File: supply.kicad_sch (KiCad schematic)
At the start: 92 parts, among them J6 205338-0004, J8 282834-4, Q5 PJE138K, Q6 SSM3J332R, Q8 PJE138K, SW1 SW_SPDT, U1 TPS56C230, U12 74LVC1G08, U13 74HCS74, U16 NTS0102, U17 SN74LV1T32DCKR, U29 TPS56C230, U41 NCP730BMT330, U42 TPS7A0518P, U6 ADM1176-1ARMZ-R7

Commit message: route all diff pairs, length tuning
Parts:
- removed R81: 10k, Resistor_SMD:R_0603_1608Metric, symbol Device:R_Small
- removed U16: NTS0102, Argus-IC:NXP_XSON-8, symbol JetsonCarrier:NTS0102
- added U30: NTS0102, Argus-IC:NXP_XSON-8, symbol Argus-IC:NTS0102
- renumbered BTN3 to BTN2, C8 to C70, C9 to C71, C26 to C72, C109 to C73, C56 to C74, C103 to C75, C57 to C76, C5 to C77, C58 to C78, C59 to C79, C65 to C80, C6 to C81, C76 to C82, C93 to C83, C77 to C84, C7 to C85, C105 to C86, C83 to C87, C102 to C88, C104 to C89, C106 to C90, C78 to C91, C80 to C92, C81 to C93, C82 to C94, C84 to C95, C85 to C96, C107 to C97, C90 to C98, C91 to C99, D7 to D19, D14 to D20, D16 to D21, D27 to D22, D25 to D23, D28 to D24, D26 to D25, J8 to J15, J6 to J16, Q8 to Q4, R14 to R104, R115 to R105, R1 to R106, R148 to R107, R25 to R108, R155 to R109, R62 to R110, R91 to R111, R193 to R112, R194 to R113, R153 to R114, R191 to R115, R82 to R116, R181 to R117, R156 to R118, R157 to R119, R158 to R120, R159 to R121, R160 to R122, R161 to R123, R162 to R124, R167 to R125, R163 to R126, R164 to R127, R165 to R128, R166 to R129, R170 to R130, R171 to R131, R168 to R132, R169 to R133, R172 to R134, R173 to R135, TP23 to TP21, TP21 to TP22, TP24 to TP23, TP28 to TP24, U12 to U27, U17 to U28, U6 to U29, U13 to U31, U1 to U32, U29 to U33, U41 to U34, U42 to U35
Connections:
- net 3V3_STDB: now also U30.3 (VCC_{A}), U30.6 (OE)
- net 5V_SoM: now also U30.7 (VCC_{B})
- net GND: now also U30.2 (GND)
- net POWER_EN: now also U30.8 (B_{1})
- net POWER_EN_3V3: now also U30.5 (A_{1})
- net SLEEP/~{WAKE}: now also U30.1 (B_{2})
- net SLEEP/~{WAKE}_3V3: now also U30.4 (A_{2})

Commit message: DRC cleanup
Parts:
- U31: footprint Package_DFN_QFN:DHWQFN-14-1EP_2.5x3mm_P0.5mm_EP1x1.5mm_ThermalVias -> Package_DFN_QFN:DHWQFN-14-1EP_2.5x3mm_P0.5mm_EP1x1.5mm
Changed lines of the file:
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@@
 			)
 		)
-		(property "Footprint" "Package_DFN_QFN:DHWQFN-14-1EP_2.5x3mm_P0.5mm_EP1x1.5mm_ThermalVias"
+		(property "Footprint" "Package_DFN_QFN:DHWQFN-14-1EP_2.5x3mm_P0.5mm_EP1x1.5mm"
 			(at 245.11 67.31 0)
 			(hide yes)
@@
 			)
 		)
-		(property "Footprint" "Package_DFN_QFN:DHWQFN-14-1EP_2.5x3mm_P0.5mm_EP1x1.5mm_ThermalVias"
+		(property "Footprint" "Package_DFN_QFN:DHWQFN-14-1EP_2.5x3mm_P0.5mm_EP1x1.5mm"
 			(at 245.11 29.21 0)
 			(hide yes)
@@
 			)
 		)
-		(property "Footprint" "Package_DFN_QFN:DHWQFN-14-1EP_2.5x3mm_P0.5mm_EP1x1.5mm_ThermalVias"
+		(property "Footprint" "Package_DFN_QFN:DHWQFN-14-1EP_2.5x3mm_P0.5mm_EP1x1.5mm"
 			(at 183.515 54.61 0)
 			(hide yes)

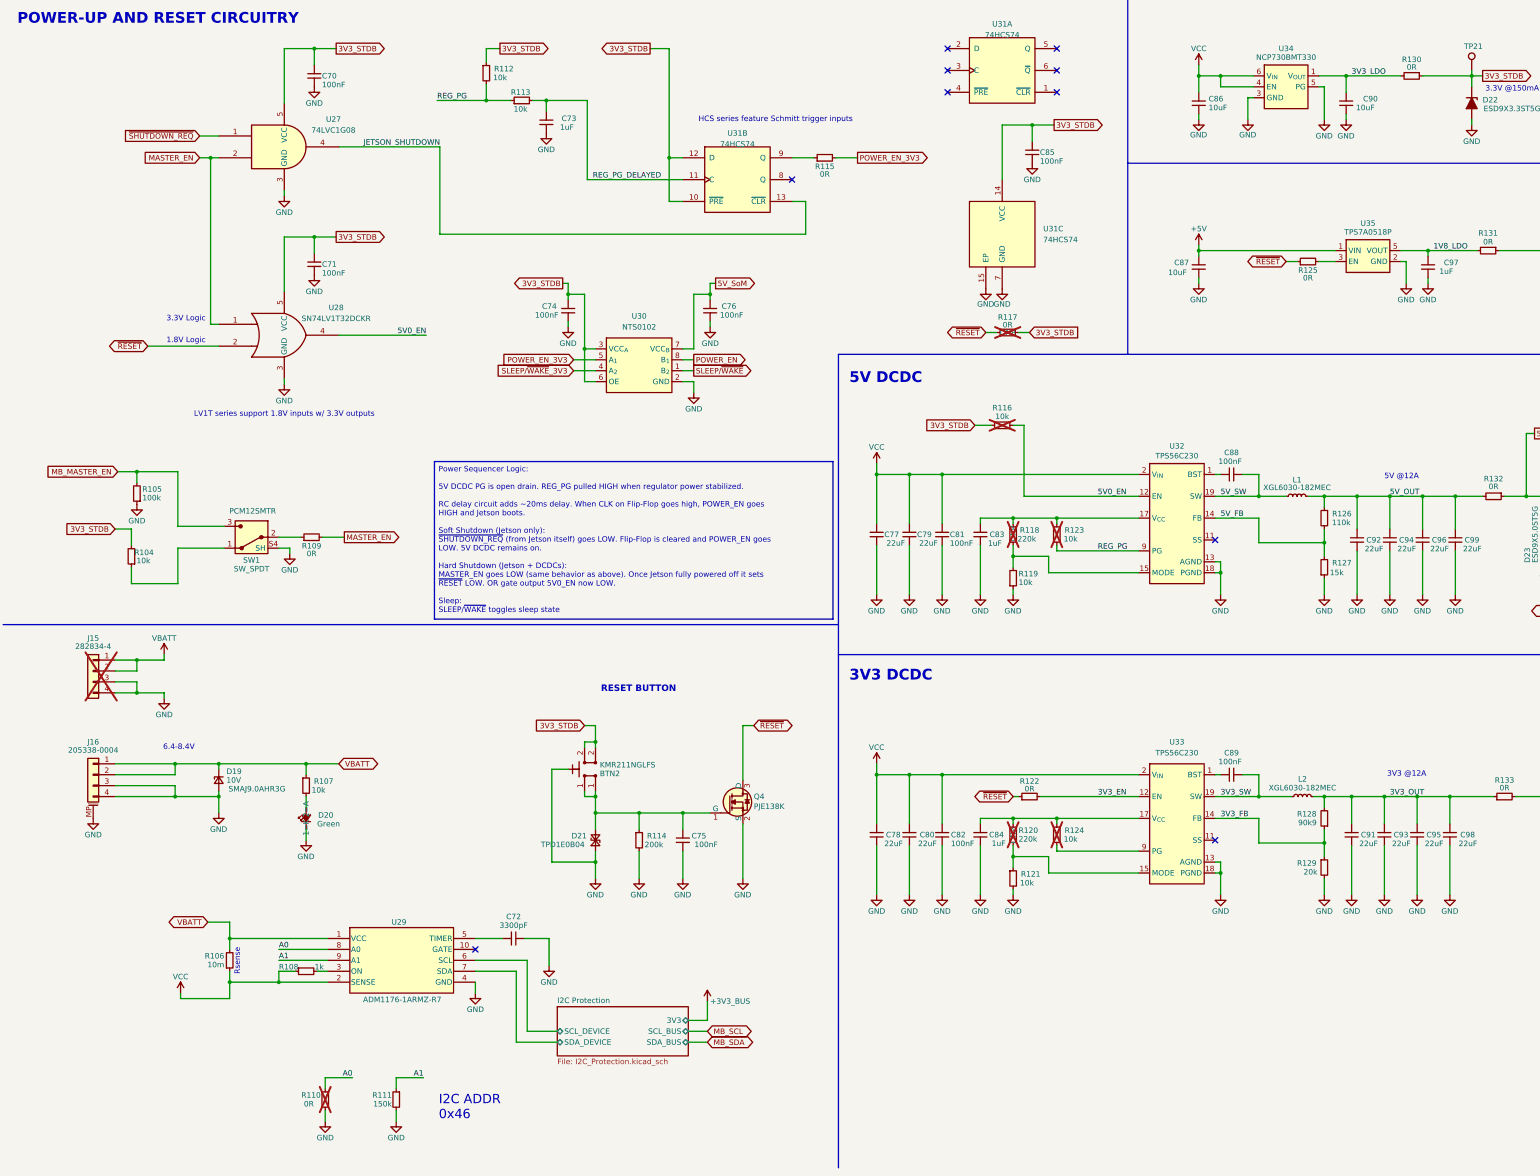
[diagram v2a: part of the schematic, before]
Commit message: Replace current monitor w/ INA226 (addr = 0x42)
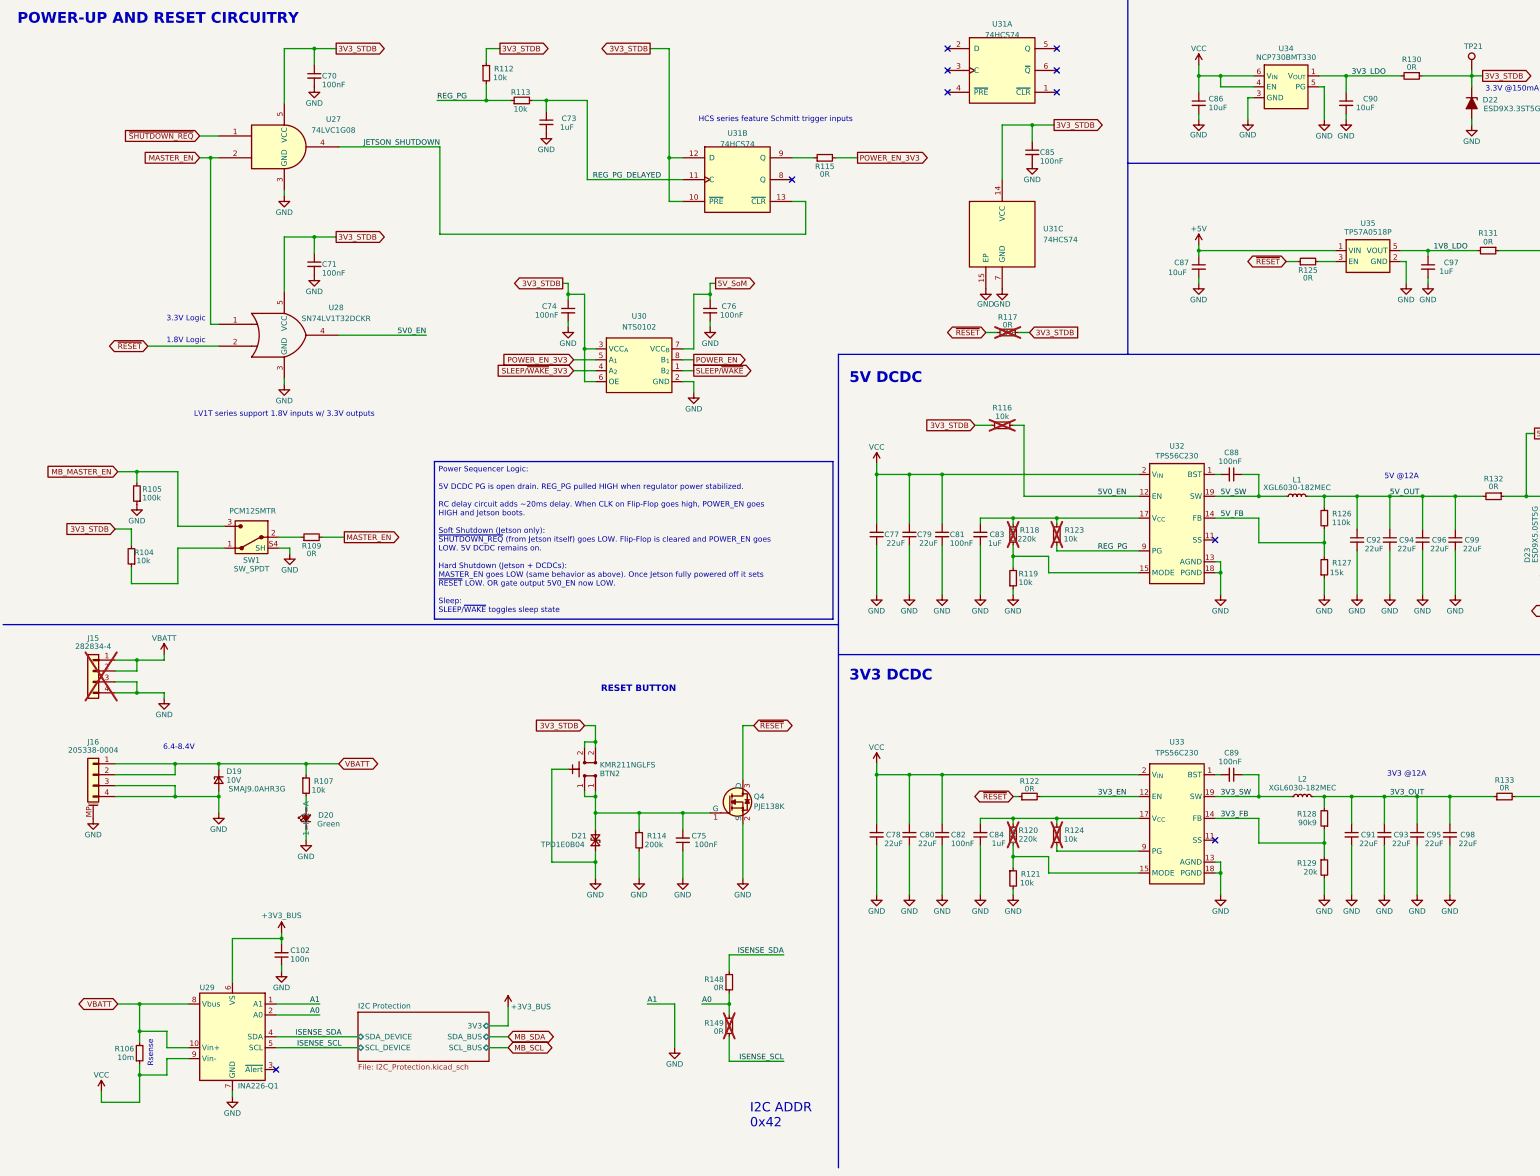
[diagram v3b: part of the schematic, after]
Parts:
- removed C72: 3300pF, Capacitor_SMD:C_0603_1608Metric, symbol Device:C_Small
- removed R108: 1k, Resistor_SMD:R_0603_1608Metric, symbol Device:R_Small
- removed R110: 0R, Resistor_SMD:R_0603_1608Metric, symbol Device:R_Small
- removed R111: 150k, Resistor_SMD:R_0603_1608Metric, symbol Device:R_Small
- removed U29: ADM1176-1ARMZ-R7, Package_SO:MSOP-10_3x3mm_P0.5mm, symbol JetsonCarrier:ADM1176-1ARMZ-R7
- added C102: 100n, Capacitor_SMD:C_0603_1608Metric, symbol Device:C_Small
- added R148, R149: 0R, Resistor_SMD:R_0603_1608Metric, symbol Device:R_Small
- added U29: INA226-Q1, Package_SO:TSSOP-10_3x3mm_P0.5mm, symbol Sensor_Energy:INA226
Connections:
- net +3V3_BUS: now also C102.2, U29.6 (VS)
- net A0: now also R148.1, R149.2, U29.2 (A0)
- net GND: now also C102.1, U29.1 (A1), U29.7 (GND)
- net VBATT: now also U29.10 (Vin+), U29.8 (Vbus)
- net VCC: now also U29.9 (Vin-)
- new net ISENSE_SCL: R149.1, U29.5 (SCL)
- new net ISENSE_SDA: R148.2, U29.4 (SDA)
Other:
- note added: "I2C ADDR 0x42"
- note removed: "I2C ADDR 0x46"
- moved on the sheet: R106

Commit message: Clean up silk, BOM
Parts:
- D20: Color Green -> Red
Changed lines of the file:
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@@
 			)
 		)
-		(property "Color" "Green"
+		(property "Color" "Red"
 			(at 91.059 204.47 90)
 			(show_name no)

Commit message: Final cleanup, production files
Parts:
- removed Q4, Q5: PJE138K, Package_TO_SOT_SMD:SOT-523, symbol JetsonCarrier:PJE138K
- added Q4, Q5: 2N7002, Package_TO_SOT_SMD:SOT-23, symbol Transistor_FET:2N7002
- C102: value 100n -> 100nF
- D24: value ESD1V8WT -> ESD5Z2.5T1G
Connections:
- net GND: now also Q4.2 (S), Q5.2 (S)
- net ~{RESET}: now also Q4.3 (D), Q5.1 (G)
- net at Q6.1 (G), R134.2: now also Q5.3 (D)
- net at BTN2.1, C75.2, D21.2 (A2)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: now also Q4.1 (G)

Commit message: Final BOM changes, gerbers
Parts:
- BTN2: LCSC (none) -> C221676
- C102, C70, C71, C74, C75, C76, C81, C82, C85, C88, C89: LCSC (none) -> C14663
- C73, C83, C84, C97: LCSC (none) -> C15849
- C77, C78, C79, C80: LCSC (none) -> C45783
- C86, C87, C90: LCSC (none) -> C96446
- C91, C92, C93, C94, C95, C96, C98, C99: LCSC (none) -> C84419
- D19: LCSC (none) -> C3720382
- D20: LCSC (none) -> C2286
- D21: LCSC (none) -> C1975594
- D22, D25: LCSC (none) -> C130456
- D23: LCSC (none) -> C87910
- D24: LCSC (none) -> C890620
- J16: LCSC (none) -> C916325
- L1, L2: value XGL6030-182MEC -> Pulse_PM2205; footprint Inductor_SMD:L_Coilcraft_XAL6030-XXX -> Argus-Passives:Pulse_PM2205; LCSC (none) -> C2638799
- Q4, Q5: LCSC (none) -> C8545
- Q6: LCSC (none) -> C146367
- R104, R107, R112, R113, R116, R119, R121, R123, R124, R134: LCSC (none) -> C25804
- R105: LCSC (none) -> C25803
- R106: LCSC (none) -> C108943
- R109, R115, R122, R125, R130, R131, R148, R149: LCSC (none) -> C21189
- R114: LCSC (none) -> C25811
- R117: LCSC (none) -> C17168
- R118, R120: LCSC (none) -> C22961
- R126: LCSC (none) -> C25574
- R127: LCSC (none) -> C22809
- R128: LCSC (none) -> C23129
- R129: LCSC (none) -> C4184
- R132, R133, R135: LCSC (none) -> C17477
- SW1: LCSC (none) -> C221841
- U27: LCSC (none) -> C7832
- U28: LCSC (none) -> C470953
- U29: LCSC (none) -> C2653835
- U30: LCSC (none) -> C2687851
- U31: LCSC (none) -> C2916506
- U32, U33: LCSC (none) -> C1849534
- U34: LCSC (none) -> C892821
- U35: LCSC (none) -> C2862322
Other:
- note added: "Switched inductor due to supply issues, original was XGL6030-182MEC"
